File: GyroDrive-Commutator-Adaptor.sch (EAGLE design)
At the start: 16 parts, among them U1 HALL, U2 PCA9517, U3 5V, U4 2.5V, U5 INA2141U, X1 NORCOMP-DB25-SMD-MALE

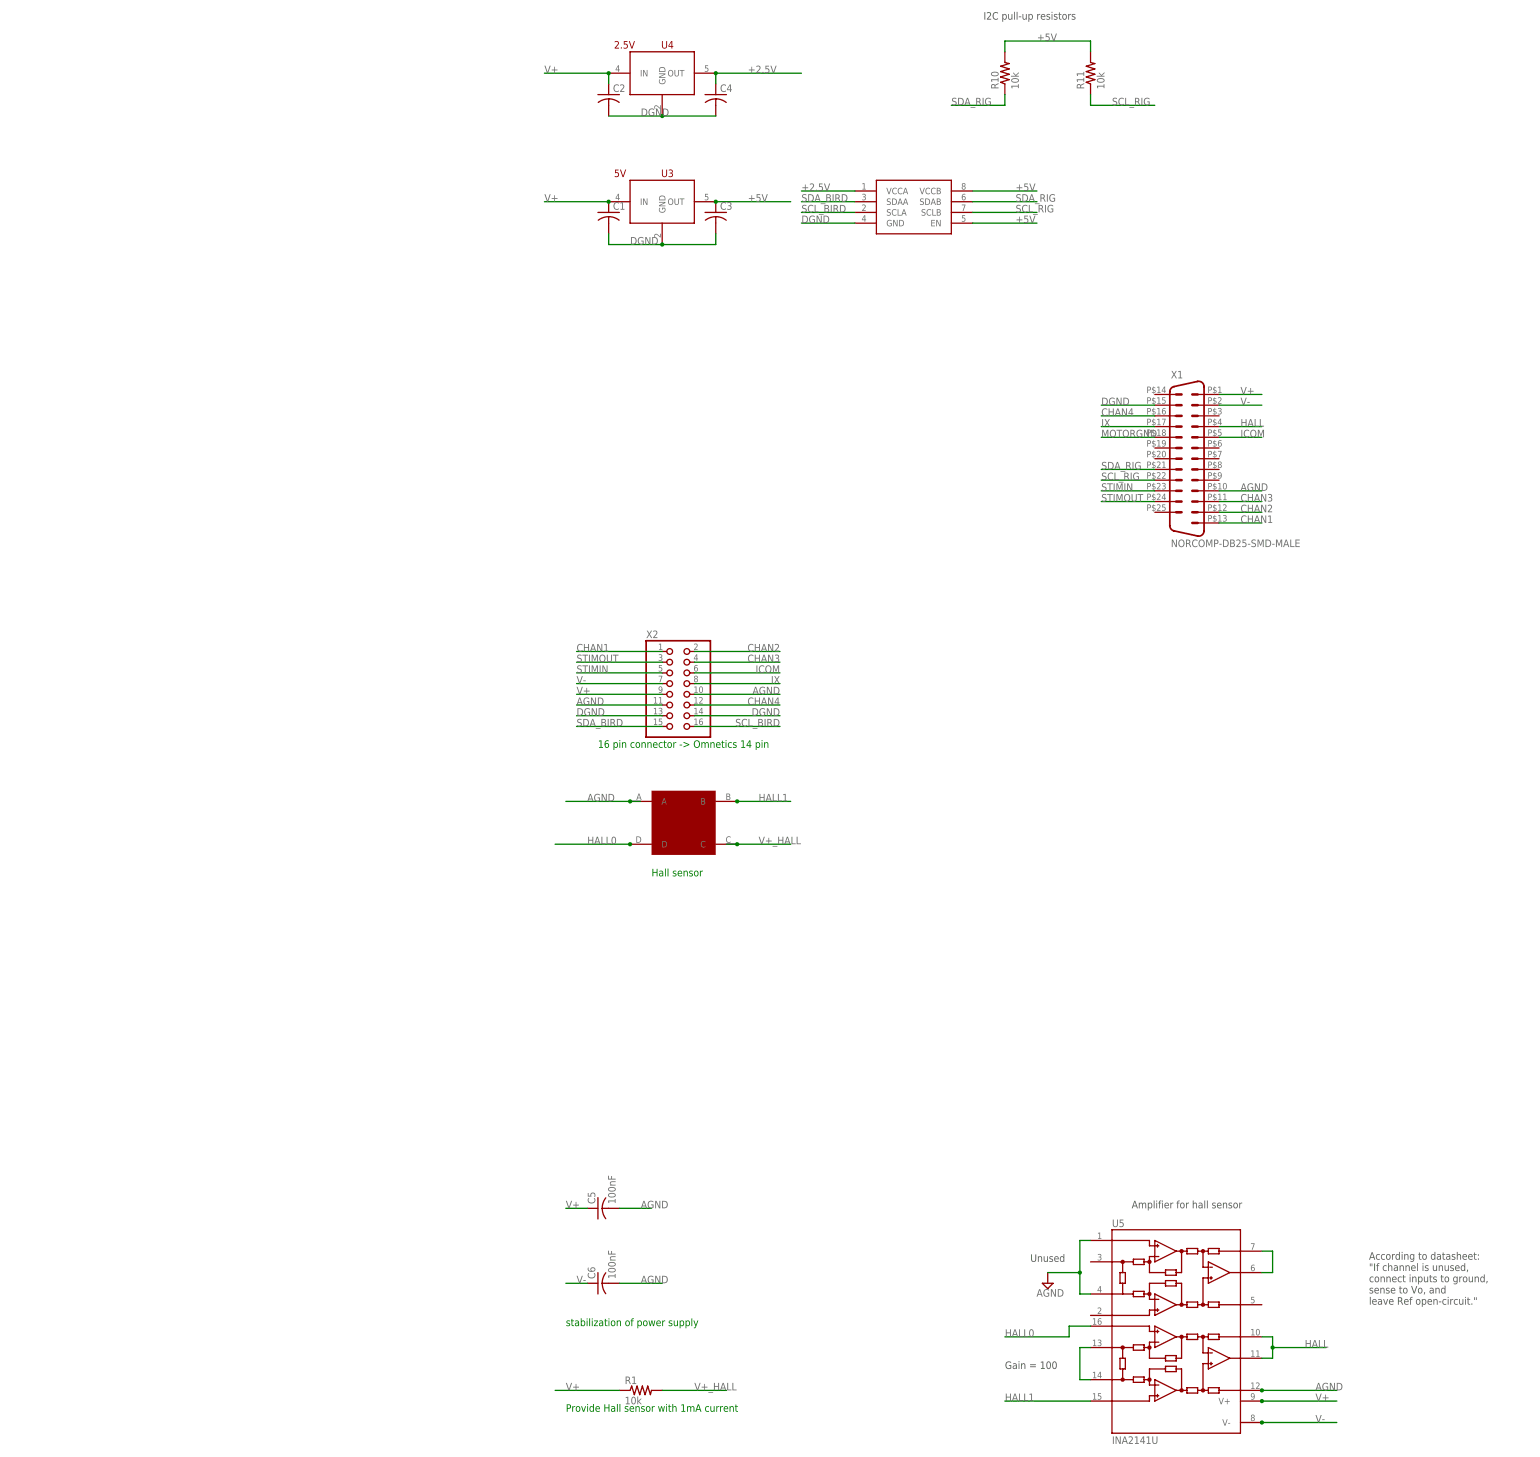
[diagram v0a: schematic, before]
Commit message: redesign as an arduino shield
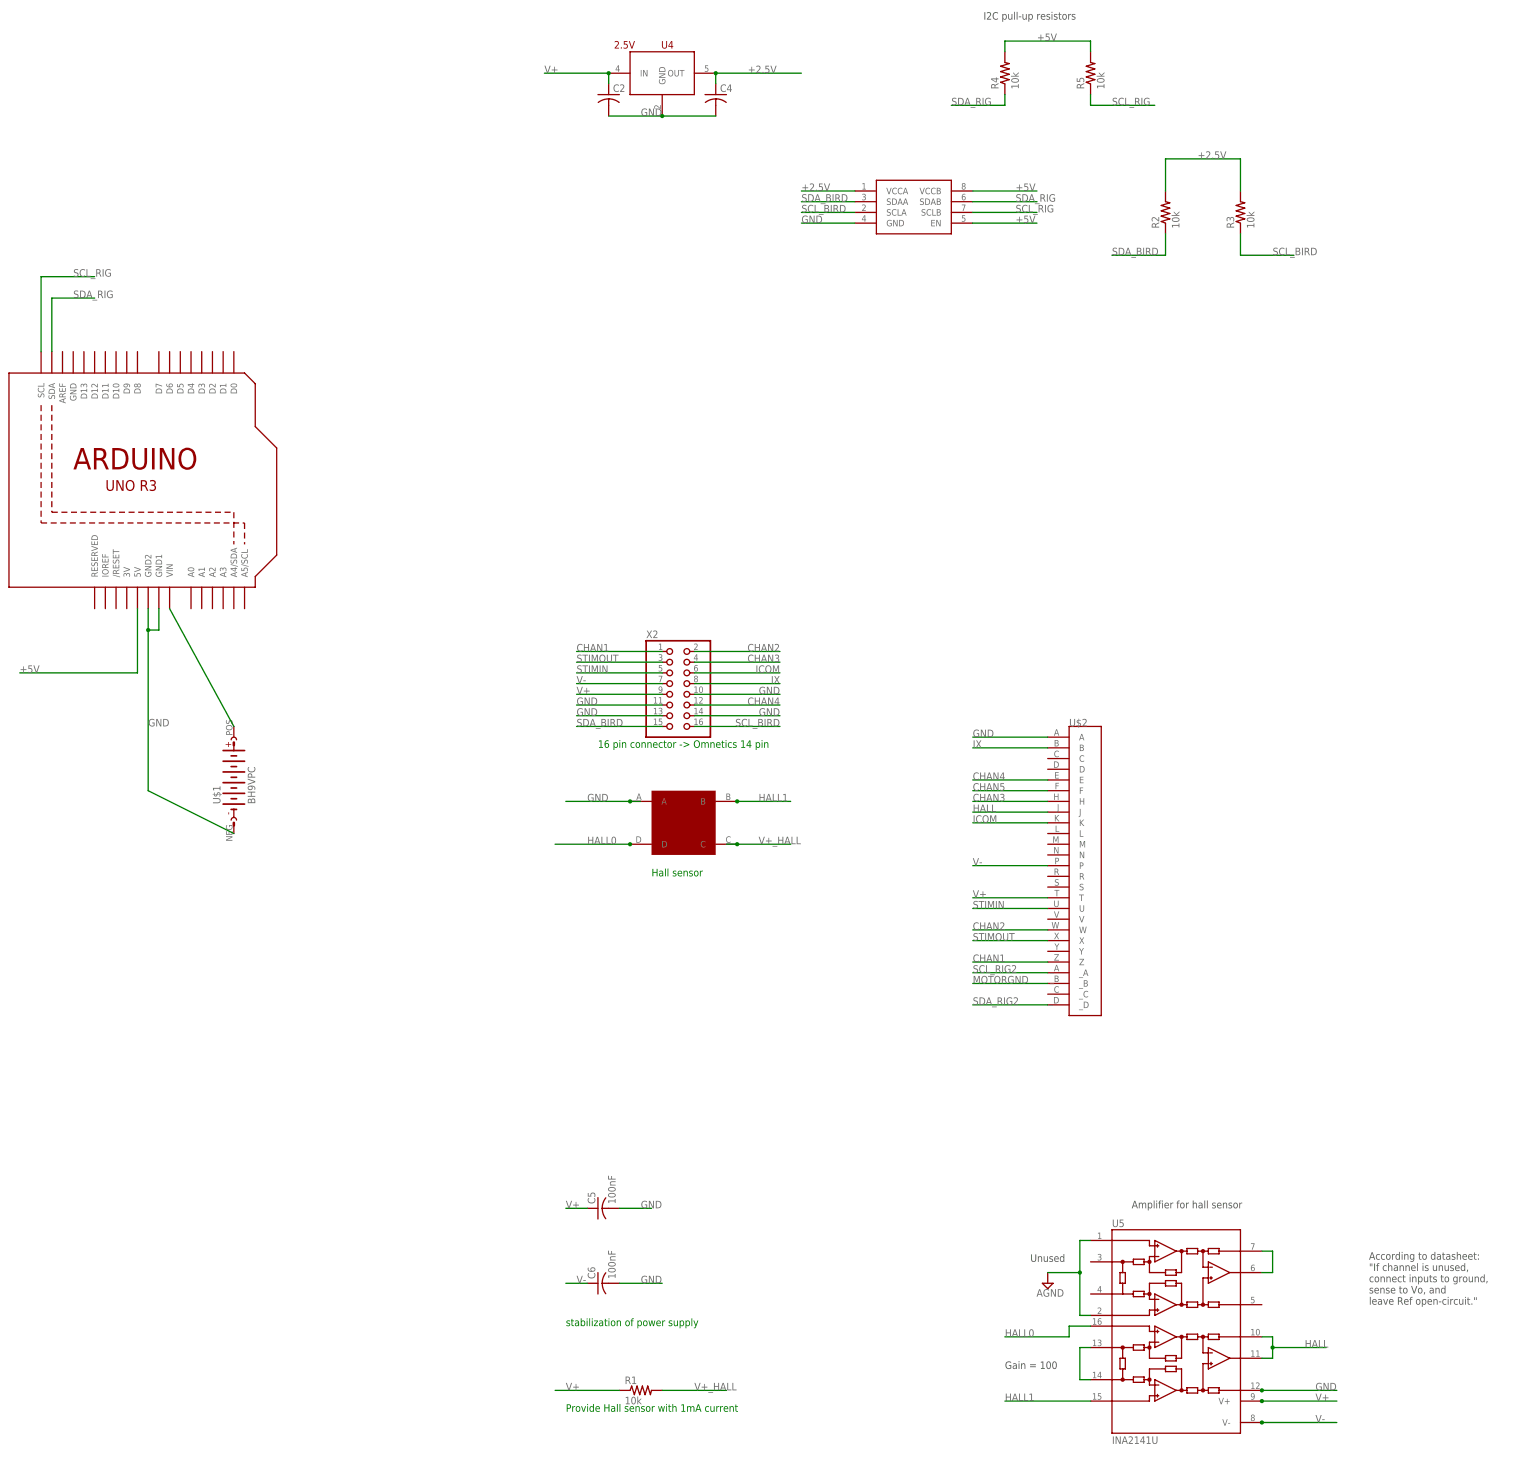
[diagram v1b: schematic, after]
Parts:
- removed C1, C3: (no value), resistor:C-USC0402
- removed U3: 5V, michael-stetner:TPS715-FIXED
- removed X1: NORCOMP-DB25-SMD-MALE, michael-stetner:NORCOMP-DB25-SMD-MALE
- added R2, R3: 10k, resistor:R-US_R0402
- added U$1: BH9VPC, mpd:BH9VPC
- added U$2: MMD1P22G-26-M101, db25-to-dale26:MMD1P22G-26-M101
- added U6: ARDUINOR3-DIMENSION, adafruit:ARDUINOR3-DIMENSION
- renumbered R10 to R4, R11 to R5
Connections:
- removed net AGND: C5.2, C6.2, U1.A, U5.INA-, U5.JA@1, U5.REFB, X1.10, X2.10, X2.11
- removed net DGND: C1.2, C2.2, C3.2, C4.2, U2.GND, U3.GND, U4.GND, X1.15, X2.13, X2.14
- new net +9V: U$1.POS, U6.VIN
- new net CHAN5: U$2.F
- new net GND: C2.2, C4.2, C5.2, C6.2, U$1.NEG, U$2.A, U1.A, U2.GND, U4.GND, U5.INA+, U5.INA-, U5.REFB, U6.GND1, U6.GND2, X2.10, X2.11, X2.13, X2.14
- new net SCL_RIG2: U$2._A
- new net SDA_RIG2: U$2._D
- net +2.5V: now also R2.2, R3.2
- net +5V: now also U6.5V; no longer C3.1, U3.OUT
- net CHAN1: now also U$2.Z; no longer X1.13
- net CHAN2: now also U$2.W; no longer X1.12
- net CHAN3: now also U$2.H; no longer X1.11
- net CHAN4: now also U$2.E; no longer X1.16
- net HALL: now also U$2.J; no longer X1.4
- net ICOM: now also U$2.K; no longer X1.5
- net IX: now also U$2.B; no longer X1.17
- net MOTORGND: now also U$2._B; no longer X1.18
- net SCL_BIRD: now also R3.1
- net SCL_RIG: now also U6.SCL; no longer X1.22
- net SDA_BIRD: now also R2.1
- net SDA_RIG: now also U6.SDA; no longer X1.21
- net STIMIN: now also U$2.U; no longer X1.23
- net STIMOUT: now also U$2.X; no longer X1.24
- net V+: now also U$2.T; no longer C1.1, U3.IN, X1.1
- net V-: now also U$2.P; no longer X1.2
